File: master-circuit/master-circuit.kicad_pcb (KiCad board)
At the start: 2 copper layers, 9 x 1 mm, 108 parts, among them U6 20nF 5%

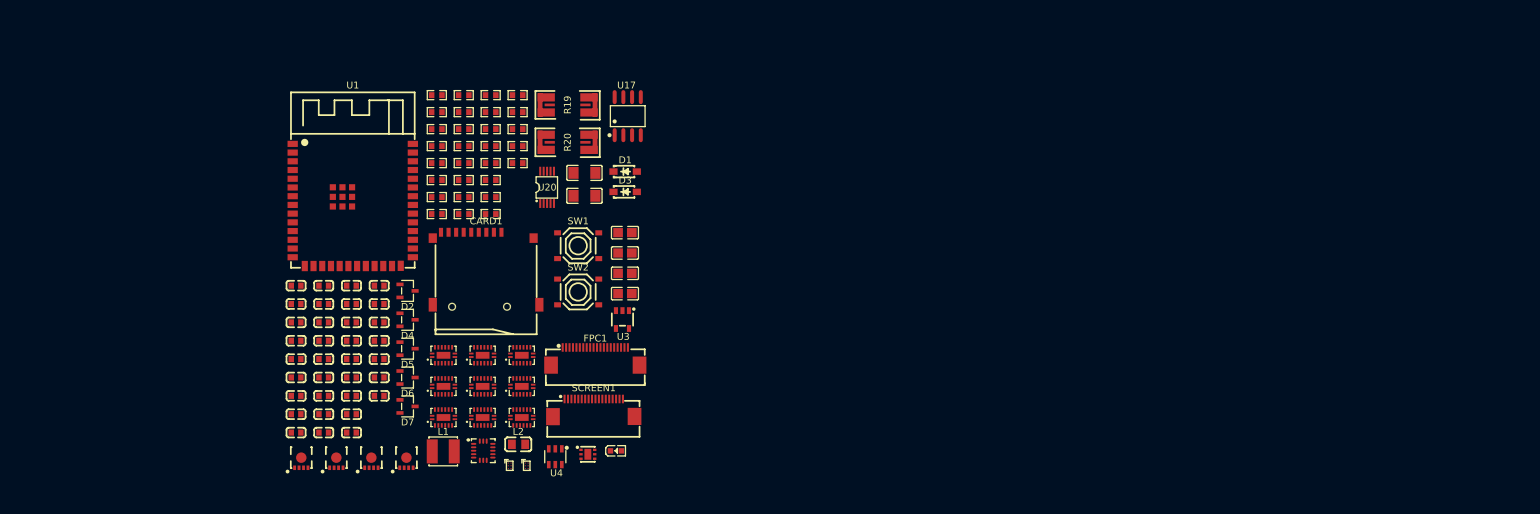
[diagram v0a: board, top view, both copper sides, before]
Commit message: Finish master controller circuit, arrange chips on the board.
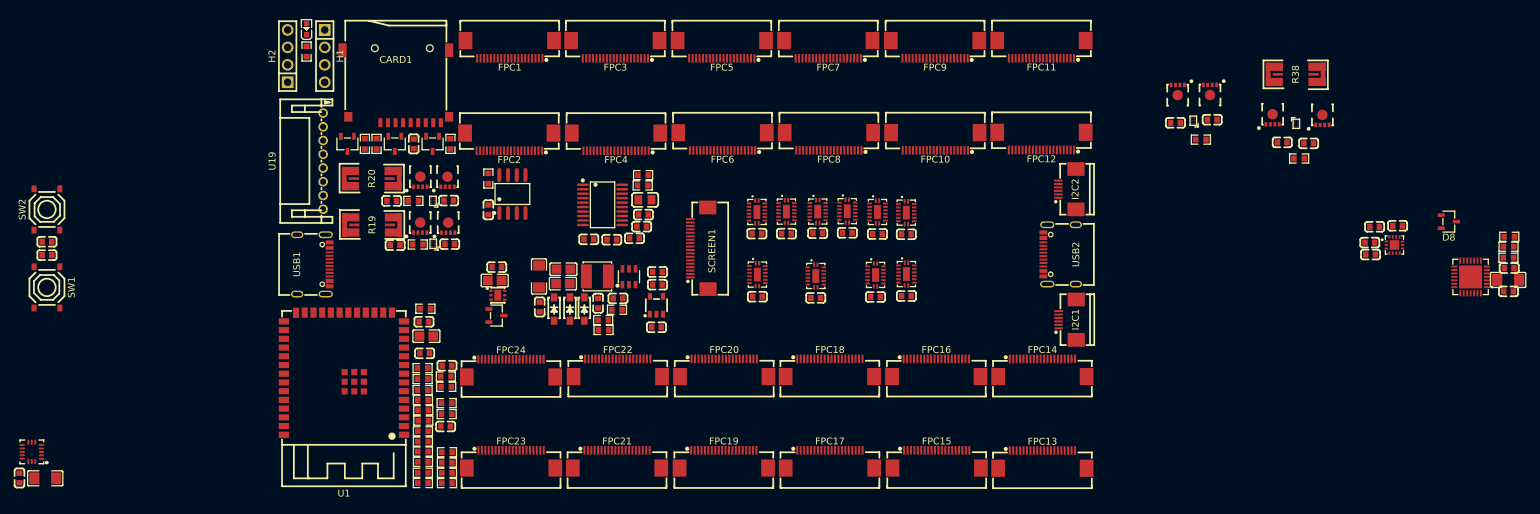
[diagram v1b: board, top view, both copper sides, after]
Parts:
- removed D5: ~, Library:SOT-23-3_L3.0-W1.7-P0.95-LS2.9-BR
- removed U14, U15, U16: ~, Library:DHVQFN-16_L3.5-W2.5-P0.50-BL-EP
- removed U20: ~, Library:VSSOP-10_L3.0-W3.0-P0.50-LS4.9-BL
- added C40: 100nF, Library:C0603, F.Cu at (165.4, 96.2)
- added C41: 100nF, Library:C0603, F.Cu at (165.4, 87.0)
- added C42: 100nF, Library:C0603, F.Cu at (169.7, 87.0)
- added C43: 100nF, Library:C0603, F.Cu at (173.9, 96.3)
- added C44: 100nF, Library:C0603, F.Cu at (174.2, 86.9)
- added C45: 100nF, Library:C0603, F.Cu at (178.5, 86.8)
- added C46: 100nF, Library:C0603, F.Cu at (182.7, 96.2)
- added C47: 100nF, Library:C0603, F.Cu at (182.9, 87.0)
- added C48: 100nF, Library:C0603, F.Cu at (187.1, 87.1)
- added C49: 1uF, Library:C0603, F.Cu at (112.7, 88.7)
- added C50: 1uF, Library:C0603, F.Cu at (241.9, 73.7)
- added C51: 1uF, Library:C0603, F.Cu at (245.7, 73.8)
- added D8: ~, Library:SOT-23-3_L3.0-W1.7-P0.95-LS2.9-BR, F.Cu at (266.1, 85.2)
- added D9: ~, Library:SOD-123_L2.7-W1.6-LS3.7-RD-1, F.Cu at (135.8, 98.0)
- added FPC10: ~, Library:FPC-SMD_20P-P0.50_XUNPU_FPC-05F-20PH20, F.Cu at (191.4, 73.5)
- added FPC11: ~, Library:FPC-SMD_20P-P0.50_XUNPU_FPC-05F-20PH20, F.Cu at (206.8, 60.1)
- added FPC12: ~, Library:FPC-SMD_20P-P0.50_XUNPU_FPC-05F-20PH20, F.Cu at (206.8, 73.5)
- added FPC13: ~, Library:FPC-SMD_20P-P0.50_XUNPU_FPC-05F-20PH20, F.Cu at (206.9, 119.8)
- added FPC14: ~, Library:FPC-SMD_20P-P0.50_XUNPU_FPC-05F-20PH20, F.Cu at (206.9, 106.5)
- added FPC15: ~, Library:FPC-SMD_20P-P0.50_XUNPU_FPC-05F-20PH20, F.Cu at (191.6, 119.8)
- added FPC16: ~, Library:FPC-SMD_20P-P0.50_XUNPU_FPC-05F-20PH20, F.Cu at (191.5, 106.5)
- added FPC17: ~, Library:FPC-SMD_20P-P0.50_XUNPU_FPC-05F-20PH20, F.Cu at (176.0, 119.8)
- added FPC18: ~, Library:FPC-SMD_20P-P0.50_XUNPU_FPC-05F-20PH20, F.Cu at (176.0, 106.5)
- added FPC19: ~, Library:FPC-SMD_20P-P0.50_XUNPU_FPC-05F-20PH20, F.Cu at (160.6, 119.8)
- added FPC2: ~, Library:FPC-SMD_20P-P0.50_XUNPU_FPC-05F-20PH20, F.Cu at (129.3, 73.6)
- added FPC20: ~, Library:FPC-SMD_20P-P0.50_XUNPU_FPC-05F-20PH20, F.Cu at (160.6, 106.5)
- added FPC21: ~, Library:FPC-SMD_20P-P0.50_XUNPU_FPC-05F-20PH20, F.Cu at (145.0, 119.8)
- added FPC22: ~, Library:FPC-SMD_20P-P0.50_XUNPU_FPC-05F-20PH20, F.Cu at (145.1, 106.5)
- added FPC23: ~, Library:FPC-SMD_20P-P0.50_XUNPU_FPC-05F-20PH20, F.Cu at (129.6, 119.8)
- added FPC24: ~, Library:FPC-SMD_20P-P0.50_XUNPU_FPC-05F-20PH20, F.Cu at (129.6, 106.5)
- added FPC3: ~, Library:FPC-SMD_20P-P0.50_XUNPU_FPC-05F-20PH20, F.Cu at (144.8, 60.2)
- added FPC4: ~, Library:FPC-SMD_20P-P0.50_XUNPU_FPC-05F-20PH20, F.Cu at (144.9, 73.6)
- added FPC5: ~, Library:FPC-SMD_20P-P0.50_XUNPU_FPC-05F-20PH20, F.Cu at (160.3, 60.2)
- added FPC6: ~, Library:FPC-SMD_20P-P0.50_XUNPU_FPC-05F-20PH20, F.Cu at (160.4, 73.6)
- added FPC7: ~, Library:FPC-SMD_20P-P0.50_XUNPU_FPC-05F-20PH20, F.Cu at (175.8, 60.2)
- added FPC8: ~, Library:FPC-SMD_20P-P0.50_XUNPU_FPC-05F-20PH20, F.Cu at (175.9, 73.5)
- added FPC9: ~, Library:FPC-SMD_20P-P0.50_XUNPU_FPC-05F-20PH20, F.Cu at (191.3, 60.2)
- added H1: ~, Library:HDR-TH_4P-P2.54-V-M, F.Cu at (102.5, 61.1)
- added H2: ~, Library:HDR-TH_4P-P2.54-V-M, F.Cu at (97.0, 61.1)
- added I2C1: ~, Library:FPC-SMD_6P-P0.50_XUNPU_FPC-05F-6PH20, F.Cu at (210.6, 99.5)
- added I2C2: ~, Library:FPC-SMD_6P-P0.50_XUNPU_FPC-05F-6PH20, F.Cu at (210.6, 80.5)
- added Q5: ~, Library:WDFN-5_L3.1-W3.1-P0.65-BL_1, F.Cu at (120.4, 86.1)
- added Q6: ~, Library:WDFN-5_L3.1-W3.1-P0.65-BL_1, F.Cu at (116.3, 86.1)
- added Q7: ~, Library:WDFN-5_L3.1-W3.1-P0.65-BL_1, F.Cu at (240.5, 70.3)
- added Q8: ~, Library:WDFN-5_L3.1-W3.1-P0.65-BL_1, F.Cu at (247.7, 70.4)
- added R32: 10kΩ, Library:R0603, F.Cu at (116.7, 109.8)
- added R33: 10kΩ, Library:R0603, F.Cu at (116.7, 108.2)
- added R34: 10kΩ, Library:R0603, F.Cu at (115.4, 82.2)
- added R35: 10kΩ, Library:R0603, F.Cu at (230.0, 73.3)
- added R36: 10kΩ, Library:R0603, F.Cu at (116.0, 88.5)
- added R37: 10kΩ, Library:R0603, F.Cu at (244.3, 76.0)
- added R38: 5mΩ, Library:R2512 Shunt with Kelvin connections, F.Cu at (243.8, 63.8)
- added R39: 1.5kΩ, Library:R0603, F.Cu at (274.8, 90.5)
- added R40: 20kΩ, Library:R0603, F.Cu at (274.8, 88.9)
- added R41: 47kΩ, Library:R0603, F.Cu at (274.9, 87.4)
- added U19: ~, Library:CONN-TH_S8B-PH-K-S-LF-SN, F.Cu at (102.2, 76.4)
- added U21: ~, Library:DHVQFN-16_L3.5-W2.5-P0.50-BL-EP, F.Cu at (165.4, 92.9)
- added U22: ~, Library:DHVQFN-16_L3.5-W2.5-P0.50-BL-EP, F.Cu at (165.4, 83.8)
- added U23: ~, Library:DHVQFN-16_L3.5-W2.5-P0.50-BL-EP, F.Cu at (169.7, 83.8)
- added U24: ~, Library:DHVQFN-16_L3.5-W2.5-P0.50-BL-EP, F.Cu at (173.9, 93.1)
- added U25: ~, Library:DHVQFN-16_L3.5-W2.5-P0.50-BL-EP, F.Cu at (174.2, 83.8)
- added U26: ~, Library:DHVQFN-16_L3.5-W2.5-P0.50-BL-EP, F.Cu at (178.5, 83.7)
- added U27: ~, Library:DHVQFN-16_L3.5-W2.5-P0.50-BL-EP, F.Cu at (182.7, 93.0)
- added U28: ~, Library:DHVQFN-16_L3.5-W2.5-P0.50-BL-EP, F.Cu at (182.9, 83.8)
- added U29: ~, Library:DHVQFN-16_L3.5-W2.5-P0.50-BL-EP, F.Cu at (187.1, 83.9)
- added USB1: ~, Library:USB-C-SMD_TYPE-C16PIN, F.Cu at (100.8, 91.5)
- added USB2: ~, Library:USB-C-SMD_TYPE-C16PIN, F.Cu at (209.4, 90.0)
- C17: value 100nF -> 10uF; footprint Library:C0603 -> Library:C1206
- C18, C29: value 100nF -> 1uF
- C27, C28: value 100nF -> 330pF
- U10: footprint Library:DHVQFN-16_L3.5-W2.5-P0.50-BL-EP -> Library:QFN-28_L5.0-W5.0-P0.50-TL-EP3.3
- U11: footprint Library:DHVQFN-16_L3.5-W2.5-P0.50-BL-EP -> Library:TSSOP-20_L6.5-W4.4-P0.65-LS6.4-BL
- U12, U13: footprint Library:DHVQFN-16_L3.5-W2.5-P0.50-BL-EP -> Library:WLCSP-6_L1.2-W0.8-P0.40-TL
- U9: footprint Library:DHVQFN-16_L3.5-W2.5-P0.50-BL-EP -> Library:QFN-14_L2.5-W2.5-P0.50-TL-EP1.4
- moved C18 173.9 mm to (274.9, 92.0), turned to 180 degrees
- moved C17 173.3 mm to (274.8, 93.7), turned to 180 degrees
- moved C16 173.0 mm to (274.8, 95.4), turned to 180 degrees
- moved C26 153.3 mm to (258.7, 85.8)
- moved U10 151.0 mm to (269.3, 93.3), turned to 180 degrees
- moved C25 149.6 mm to (255.3, 86.0)
- moved C28 149.5 mm to (254.7, 90.0)
- moved C27 149.3 mm to (254.6, 88.3)
- moved U9 140.0 mm to (258.2, 88.6)
- moved Q3 129.3 mm to (226.7, 66.1), turned to 180 degrees
- moved Q4 129.0 mm to (231.4, 66.0), turned to 180 degrees
- moved C38 127.0 mm to (231.7, 70.4), turned to 180 degrees
- moved U13 126.0 mm to (243.9, 71.0)
- moved C39 122.6 mm to (226.3, 70.8), turned to 180 degrees
- moved U7 109.3 mm to (228.9, 70.5), turned to 180 degrees
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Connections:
- C15 pad 1: Net-(U9-EP) -> GND
- C16 pad 1: Net-(U8-EP) -> GND
- C17 pad 1: Net-(U10-EP) -> GND
- C18 pad 1: Net-(U11-EP) -> Net-(U10-VBUS)
- C18 pad 2: 3V3 -> GND
- C25 pad 1: Net-(U12-EP) -> GND
- C26 pad 1: Net-(U13-EP) -> GND
- C27 pad 1: Net-(U14-EP) -> GND
- C27 pad 2: 3V3 -> SENSORS_CC1
- C28 pad 1: Net-(U15-EP) -> GND
- C28 pad 2: 3V3 -> SENSORS_CC2
- C29 pad 1: Net-(U16-EP) -> GND
- C29 pad 2: 3V3 -> VCC
- C36 pad 2: VBUS -> VCC
- C37 pad 2: VCC -> VBATTERY
- C38 pad 2: VCC -> SENSORS_VBUS
- C39 pad 2: VBATTERY -> VCC
- D4 pad 1: Net-(CARD1-DAT1(RSV)) -> FSPICS0/MEMORY_CS
- FPC1 pad 13: CS -> /group-of-8-servo-connectors/master-to-servo-connector/SERVO_CS
- FPC1 pad 14: SPI3_SCK -> SPI3_CLK
- FPC1 pad 19: BOOT0/STOP -> /group-of-8-servo-connectors/master-to-servo-connector/SERVO_BOOT0/STOP
- FPC1 pad 20: NRST -> /group-of-8-servo-connectors/master-to-servo-connector/SERVO_NRST
- Q1 pad 1: VBUS -> VCC
- Q1 pad 2: VBUS -> VCC
- Q1 pad 3: VBUS -> VCC
- Q2 pad 1: VCC -> VBATTERY
- Q2 pad 2: VCC -> VBATTERY
- Q2 pad 3: VCC -> VBATTERY
- Q3 pad 1: VBATTERY -> SENSORS_VBUS
- Q3 pad 2: VBATTERY -> SENSORS_VBUS
- Q3 pad 3: VBATTERY -> SENSORS_VBUS
- U1 pad 12: STATUS_LED -> SENSOR_CURRENT
- U1 pad 28: IMU_INTERRUPT -> STATUS_LED
- U10 pad 10: 3V3 -> unconnected-(U10-NC-Pad10)
- U10 pad 11: FSPICLK/SPI2_CLK -> unconnected-(U10-SUSPENDb-Pad11)
- U10 pad 12: SHIFT_BANK1_LATCH -> unconnected-(U10-SUSPEND-Pad12)
- U10 pad 13: SHIFT_OE -> unconnected-(U10-CHREN-Pad13)
- U10 pad 14: Net-(U10-SER) -> unconnected-(U10-CHR1-Pad14)
- U10 pad 16: 3V3 -> unconnected-(U10-GPIO.3/WAKEUP-Pad16)
- U10 pad 17: Net-(U10-EP) -> unconnected-(U10-GPIO.2/RS485-Pad17)
- U10 pad 3: unconnected-(U10-Q3-Pad3) -> GND
- U10 pad 4: unconnected-(U10-Q4-Pad4) -> SENSORS_USB_D+
- U10 pad 5: unconnected-(U10-Q5-Pad5) -> SENSORS_USB_D-
- U10 pad 6: unconnected-(U10-Q6-Pad6) -> 3V3
- U10 pad 7: unconnected-(U10-Q7-Pad7) -> 3V3
- U10 pad 8: Net-(U10-EP) -> Net-(U10-VBUS)
- U10 pad 9: Net-(U10-Q7S) -> Net-(U10-RSTb)
- U11 pad 1: unconnected-(U11-Q1-Pad1) -> REFERENCE
- U11 pad 10: 3V3 -> unconnected-(U11-NC-Pad10)
- U11 pad 11: FSPICLK/SPI2_CLK -> unconnected-(U11-NC-Pad11)
- U11 pad 12: SHIFT_BANK1_LATCH -> REFERENCE
- U11 pad 13: SHIFT_OE -> SENSOR_CURRENT
- U11 pad 14: Net-(U10-Q7S) -> -Probe-3
- U11 pad 15: unconnected-(U11-Q0-Pad15) -> +Probe-3
- U11 pad 16: 3V3 -> GND
- U11 pad 17: Net-(U11-EP) -> unconnected-(U11-IN+4-Pad17)
- U11 pad 2: unconnected-(U11-Q2-Pad2) -> VBUS_CURRENT
- U11 pad 3: unconnected-(U11-Q3-Pad3) -> -Probe-1
- U11 pad 4: unconnected-(U11-Q4-Pad4) -> +Probe-1
- U11 pad 5: unconnected-(U11-Q5-Pad5) -> 3V3A
- U11 pad 6: unconnected-(U11-Q6-Pad6) -> +Probe-2
- U11 pad 7: unconnected-(U11-Q7-Pad7) -> -Probe-2
- U11 pad 8: Net-(U11-EP) -> BATTERY_CURRENT
- U11 pad 9: unconnected-(U11-Q7S-Pad9) -> REFERENCE
- U18 pad 11: IMU_INTERRUPT -> unconnected-(U18-INT1-Pad11)
- U2 pad A1: Net-(Q1-G) -> Net-(Q2-G)
- U2 pad A2: VBUS -> VBATTERY
- U2 pad B1: Net-(Q2-G) -> Net-(Q1-G)
- U2 pad C2: CONNECT_VBUS -> CONNECT_BATTERY
- U7 pad A1: Net-(Q3-G) -> Net-(Q4-G)
- U7 pad A2: VBATTERY -> VCC
- U7 pad B1: Net-(Q4-G) -> Net-(Q3-G)
- U7 pad C1: VCC -> SENSORS_VBUS
- U7 pad C2: CONNECT_BATTERY -> CONNECT_SENSORS_VCC
- U8 pad 1: unconnected-(U8-Q1-Pad1) -> I2C1_BOOT0/STOP
- U8 pad 11: SPI3_CLK -> FSPICLK/SPI2_CLK
- U8 pad 14: SPI3_MOSI -> SHIFT_BANK_2_DATA_CONT
- U8 pad 15: unconnected-(U8-Q0-Pad15) -> I2C1_NRST
- U8 pad 17: Net-(U8-EP) -> GND
- U8 pad 2: unconnected-(U8-Q2-Pad2) -> I2C2_NRST
- U8 pad 3: unconnected-(U8-Q3-Pad3) -> I2C2_BOOT0/STOP
- U8 pad 4: unconnected-(U8-Q4-Pad4) -> SENSOR_NRST
- U8 pad 5: unconnected-(U8-Q5-Pad5) -> SENSOR_BOOT0/STOP
- U8 pad 6: unconnected-(U8-Q6-Pad6) -> CONNECT_SENSORS_5V
- U8 pad 7: unconnected-(U8-Q7-Pad7) -> CONNECT_SENSORS_VCC
- U8 pad 8: Net-(U8-EP) -> GND
- U8 pad 9: Net-(U12-SER) -> unconnected-(U8-Q7S-Pad9)
- U9 pad 1: unconnected-(U9-Q1-Pad1) -> SENSORS_CC2
- U9 pad 10: 3V3 -> SENSORS_CC1
- U9 pad 11: FSPICLK/SPI2_CLK -> SENSORS_CC1
- U9 pad 12: SHIFT_BANK1_LATCH -> 3V3
- U9 pad 13: SHIFT_OE -> 3V3
- U9 pad 14: FSPID/SPI2_MOSI -> SENSORS_CC2
- U9 pad 15: unconnected-(U9-Q0-Pad15) -> GND
- U9 pad 2: unconnected-(U9-Q2-Pad2) -> SENSORS_VBUS
- U9 pad 3: unconnected-(U9-Q3-Pad3) -> 3V3
- U9 pad 4: unconnected-(U9-Q4-Pad4) -> 3V3
- U9 pad 6: unconnected-(U9-Q6-Pad6) -> I2C2_SCL
- U9 pad 7: unconnected-(U9-Q7-Pad7) -> I2C2_SDA
- U9 pad 8: Net-(U9-EP) -> unconnected-(U9-NC-Pad8)
- U9 pad 9: Net-(U10-SER) -> GND

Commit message: Partially wire up control circuit.
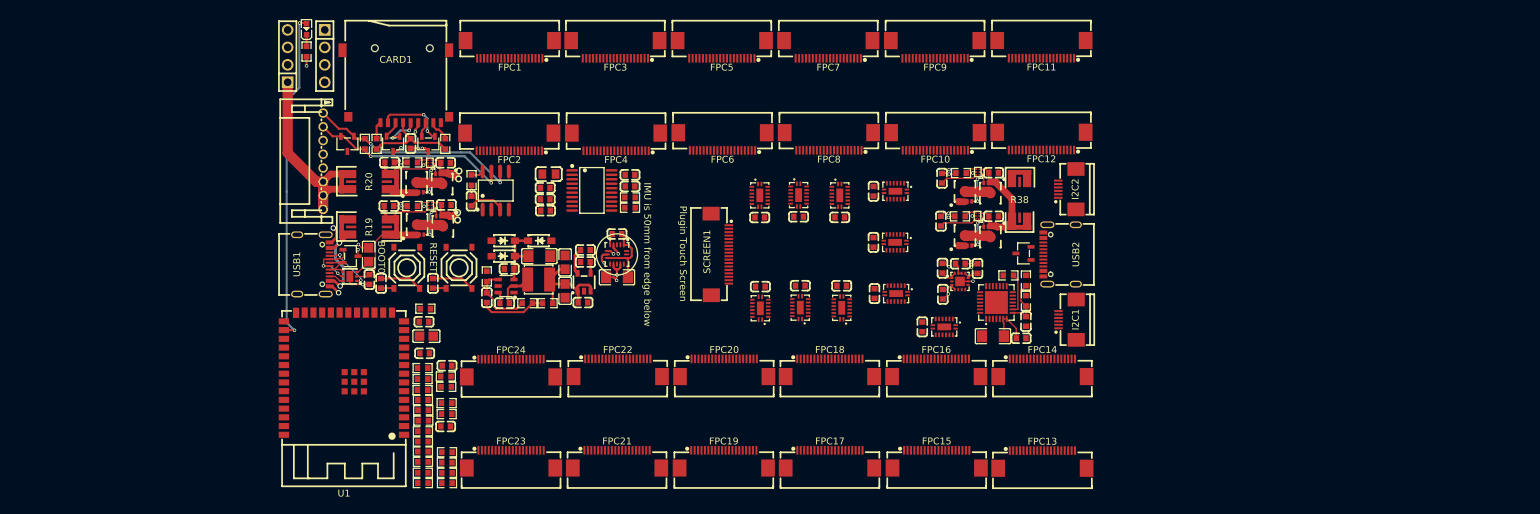
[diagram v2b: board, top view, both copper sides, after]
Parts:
- moved C31 94.0 mm to (145.0, 87.0), turned to 0 degrees
- moved U18 89.9 mm to (145.0, 90.0), turned to -90 degrees
- moved C32 88.2 mm to (145.0, 93.3), turned to 0 degrees
- moved C17 75.5 mm to (199.8, 101.9), turned to 0 degrees
- moved R39 72.9 mm to (202.0, 93.1), turned to 0 degrees
- moved C16 71.3 mm to (203.8, 102.2)
- moved R41 71.0 mm to (204.6, 96.8), turned to 90 degrees
- moved C18 70.8 mm to (204.6, 99.8), turned to -90 degrees
- moved R40 70.4 mm to (204.6, 93.8), turned to -90 degrees
- moved U10 69.2 mm to (200.2, 97.0), turned to 90 degrees
- moved C26 63.9 mm to (195.0, 91.3), turned to 180 degrees
- moved C25 63.6 mm to (192.4, 95.8), turned to 90 degrees
- moved U9 63.5 mm to (194.9, 93.9)
- moved C28 62.4 mm to (192.4, 92.0), turned to -90 degrees
- moved D8 62.1 mm to (204.2, 89.8), turned to 180 degrees
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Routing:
- net GND: track 0.00 -> 58.4 mm, vias 0 -> 32
- net STATUS_LED: track 0.00 -> 48.6 mm, vias 0 -> 2
- net 3V3: track 0.00 -> 45.0 mm
- net CANL: track 0.00 -> 31.6 mm, vias 0 -> 2
- net CANH: track 0.00 -> 29.6 mm, vias 0 -> 2
- net VBATTERY_PINS: track 0.00 -> 29.2 mm
- net 5V: track 0.00 -> 23.0 mm
- net VBUS: track 0.00 -> 22.3 mm
- net VCC: track 0.00 -> 21.5 mm, vias 0 -> 4
- net SENSORS_VBUS: track 0.00 -> 17.6 mm
- net VBUS_PINS: track 0.00 -> 13.5 mm, vias 0 -> 2
- net VBATTERY: track 0.00 -> 12.4 mm
- net Buck-FB: track 0.00 -> 10.4 mm
- net FSPICS0/MEMORY_CS: track 0.00 -> 10.2 mm, vias 0 -> 2
- net /Buck-Probe-Point: track 0.00 -> 9.63 mm
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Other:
- copper layers 2 -> 4
- board text added: "BOOT0"
- board text added: "IMU Position"
- board text added: "IMU is 50mm from edge below"
- board text added: "Plugin Touch Screen"
- board text added: "RESET"

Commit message: Continue wiring control circuit.
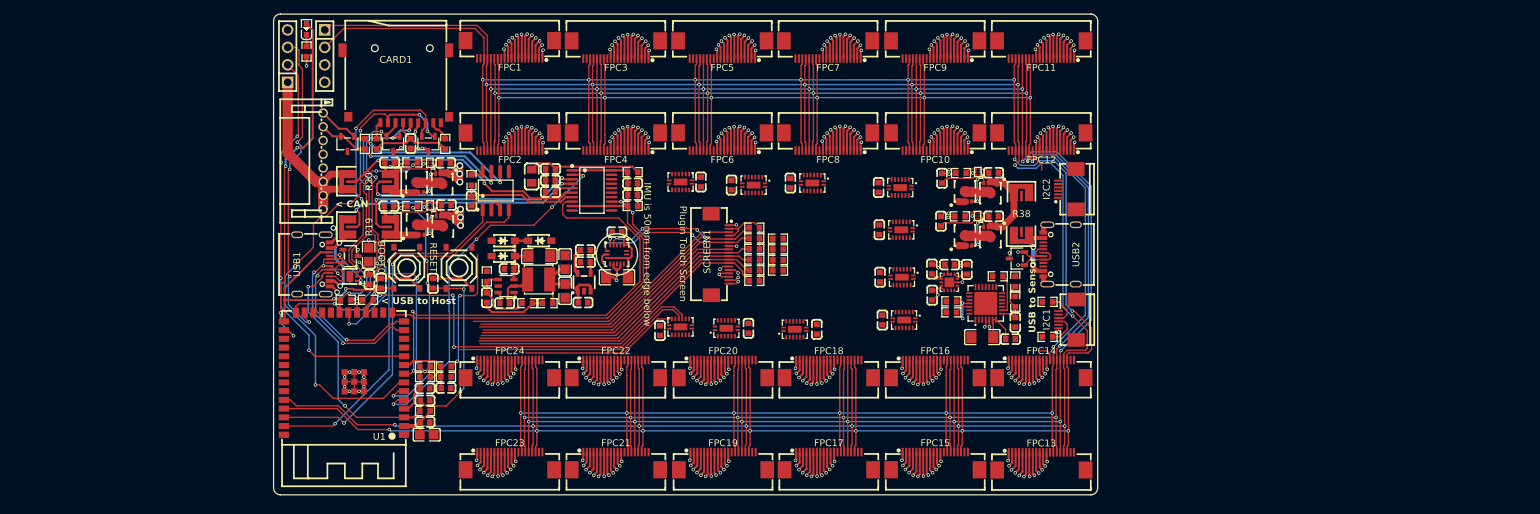
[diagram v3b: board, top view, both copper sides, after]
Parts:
- moved R24 93.5 mm to (207.7, 96.9)
- moved R25 92.2 mm to (207.7, 102.0)
- moved R32 77.8 mm to (193.7, 98.4)
- moved R33 77.8 mm to (193.7, 96.8)
- moved R17 60.0 mm to (165.0, 86.1), turned to 0 degrees
- moved R13 58.2 mm to (168.4, 87.7)
- moved R18 58.2 mm to (165.0, 87.7), turned to 0 degrees
- moved R8 56.3 mm to (165.0, 89.2), turned to 0 degrees
- moved R29 56.2 mm to (168.4, 89.2)
- moved R28 56.1 mm to (168.4, 90.8)
- moved R30 53.7 mm to (168.4, 92.3)
- moved R26 53.0 mm to (165.0, 93.8), turned to 0 degrees
- moved R27 52.9 mm to (165.0, 92.3), turned to 0 degrees
- moved R14 52.8 mm to (165.0, 90.8), turned to 0 degrees
- moved R15 29.0 mm to (105.5, 96.6), turned to 0 degrees
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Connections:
- U1 pad 11: BATTERY_2 -> SCREEN_RESET
- U1 pad 25: SCREEN_RESET -> BATTERY_2
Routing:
- net GND: track 58.4 -> 493.7 mm, vias 32 -> 196
- net TX: track 0.00 -> 430.7 mm, vias 0 -> 17
- net RX: track 0.00 -> 427.4 mm, vias 0 -> 15
- net VCC: track 21.5 -> 422.7 mm, vias 4 -> 150
- net SPI3_MOSI: track 0.00 -> 357.6 mm, vias 0 -> 14
- net SPI3_MISO: track 0.00 -> 357.2 mm, vias 0 -> 14
- net SPI3_CLK: track 0.00 -> 356.2 mm, vias 0 -> 14
- net FSPICLK/SPI2_CLK: track 5.26 -> 86.4 mm, vias 2 -> 5
- net FSPID/SPI2_MOSI: track 2.65 -> 80.6 mm, vias 0 -> 4
- net REFERENCE: track 0.00 -> 72.3 mm
- net SHIFT_BANK2_LATCH: track 0.00 -> 69.5 mm, vias 0 -> 4
- net BATTERY_CURRENT: track 0.00 -> 67.5 mm, vias 0 -> 2
- net RESET: track 1.95 -> 64.1 mm, vias 0 -> 4
- net CONNECT_BATTERY: track 1.74 -> 63.1 mm, vias 0 -> 4
- net I2C2_SCL: track 1.07 -> 61.2 mm, vias 1 -> 4
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- added copper zone on In2.Cu, net GND
- added copper zone on In1.Cu, net VCC
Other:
- board size 9 x 1 mm -> 120 x 70 mm
- board text added: "< CAN"
- board text added: "< USB to Host"
- board text added: "USB to Sensor"

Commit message: Almost wired controller.
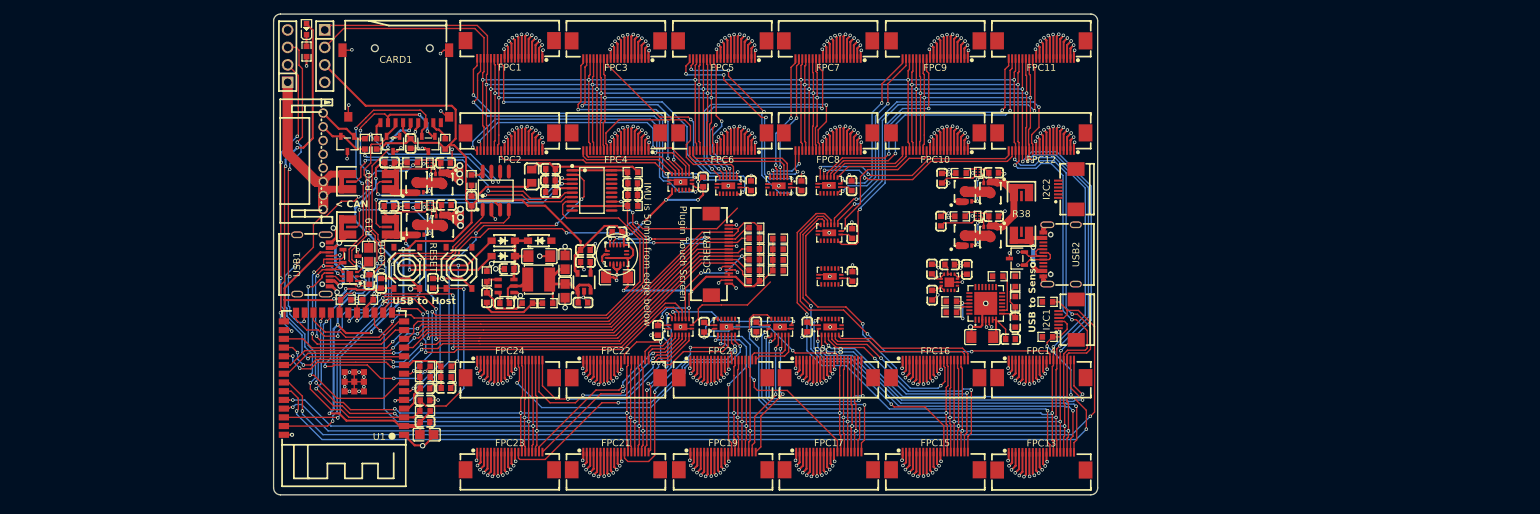
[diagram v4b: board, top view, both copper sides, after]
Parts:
- moved C45 11.0 mm to (172.7, 100.6), turned to 90 degrees
- moved U26 10.8 mm to (176.1, 100.6), turned to 0 degrees
- moved U8 10.5 mm to (176.0, 93.2)
- moved U24 10.5 mm to (175.9, 86.8)
- moved U25 10.4 mm to (175.9, 80.0)
- moved C47 8.81 mm to (165.3, 100.6)
- moved C46 6.45 mm to (157.7, 100.6)
- moved U23 4.90 mm to (168.6, 80.0)
- moved C15 4.02 mm to (179.3, 93.2)
- moved C43 4.00 mm to (179.2, 87.0)
- moved C44 3.94 mm to (179.2, 80.0)
- moved U21 3.69 mm to (161.2, 80.0)
- moved C40 2.83 mm to (164.5, 80.0)
- moved U28 2.18 mm to (168.8, 100.6)
- moved C42 1.66 mm to (171.9, 80.0)
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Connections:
- C41 pad 1: Net-(U22-EP) -> GND
- C44 pad 1: Net-(U25-EP) -> GND
- C47 pad 1: Net-(U28-EP) -> GND
- U22 pad 17: Net-(U22-EP) -> GND
- U22 pad 8: Net-(U22-EP) -> GND
- U25 pad 17: Net-(U25-EP) -> GND
- U25 pad 8: Net-(U25-EP) -> GND
- U28 pad 17: Net-(U28-EP) -> GND
- U28 pad 8: Net-(U28-EP) -> GND
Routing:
- net 3V3: track 76.4 -> 284.3 mm, vias 2 -> 13
- net I2C1_SCL: track 4.71 -> 146.2 mm, vias 0 -> 2
- net I2C1_SDA: track 4.73 -> 143.0 mm, vias 0 -> 4
- net GND: track 493.7 -> 568.1 mm, vias 196 -> 243
- net /group-of-8-servo-connectors1/master-to-servo-connector4/SERVO_CS: track 0.00 -> 69.8 mm, vias 0 -> 2
- net SHIFT_BANK1_LATCH: track 0.00 -> 62.7 mm, vias 0 -> 4
- net /group-of-8-servo-connectors1/master-to-servo-connector5/SERVO_CS: track 2.56 -> 56.2 mm, vias 0 -> 2
- net /group-of-8-servo-connectors1/master-to-servo-connector4/SERVO_BOOT0/STOP: track 0.00 -> 52.8 mm, vias 0 -> 2
- net /group-of-8-servo-connectors/master-to-servo-connector/SERVO_CS: track 0.00 -> 51.8 mm, vias 0 -> 2
- net /group-of-8-servo-connectors1/master-to-servo-connector4/SERVO_NRST: track 0.00 -> 50.9 mm, vias 0 -> 2
- net /group-of-8-servo-connectors/master-to-servo-connector/SERVO_BOOT0/STOP: track 0.00 -> 50.4 mm, vias 0 -> 2
- net /group-of-8-servo-connectors1/master-to-servo-connector6/SERVO_CS: track 0.00 -> 49.6 mm, vias 0 -> 2
- net /group-of-8-servo-connectors1/master-to-servo-connector5/SERVO_BOOT0/STOP: track 0.00 -> 49.5 mm, vias 0 -> 2
- net /group-of-8-servo-connectors1/master-to-servo-connector2/SERVO_CS: track 0.00 -> 49.5 mm, vias 0 -> 2
- net /group-of-8-servo-connectors/master-to-servo-connector/SERVO_NRST: track 0.00 -> 48.3 mm, vias 0 -> 2
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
